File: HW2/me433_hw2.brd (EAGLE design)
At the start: 50 x 50 mm, 22 parts

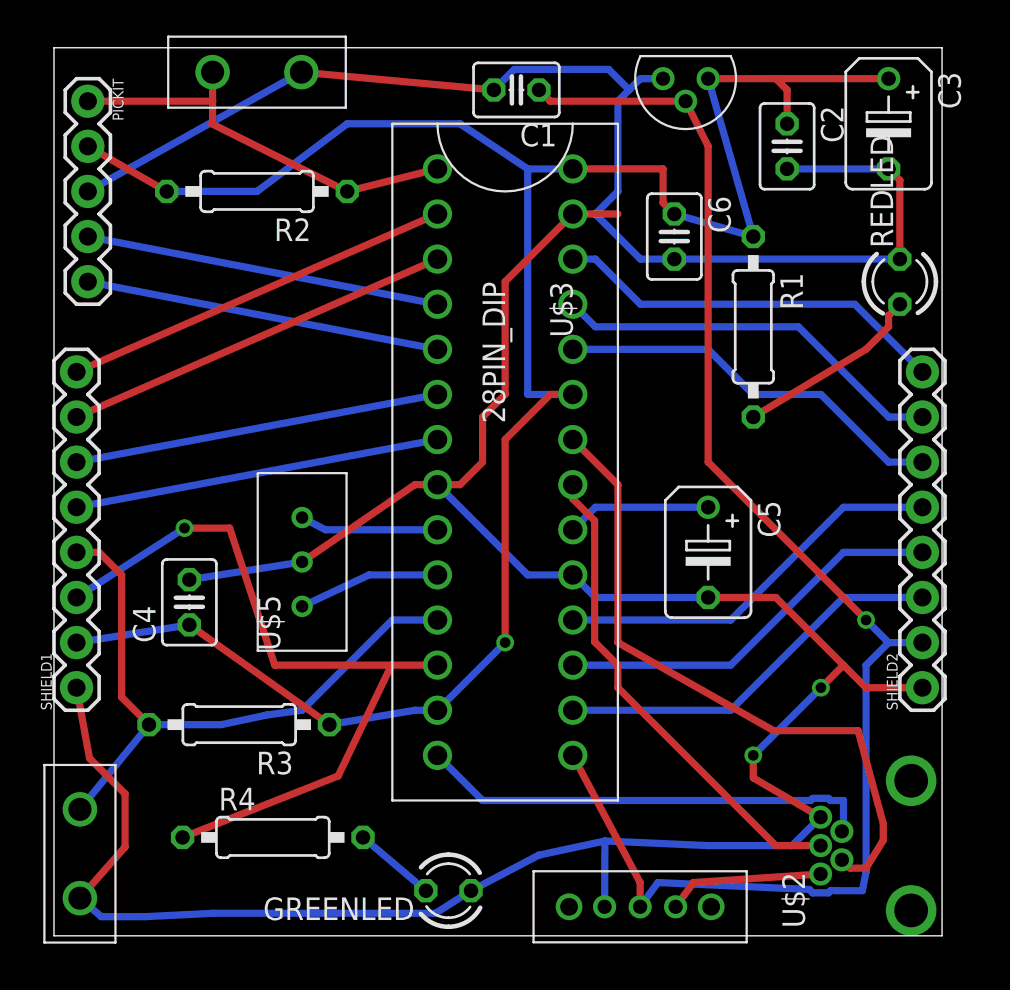
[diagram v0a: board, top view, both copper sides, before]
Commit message: added ground plane and fixed things
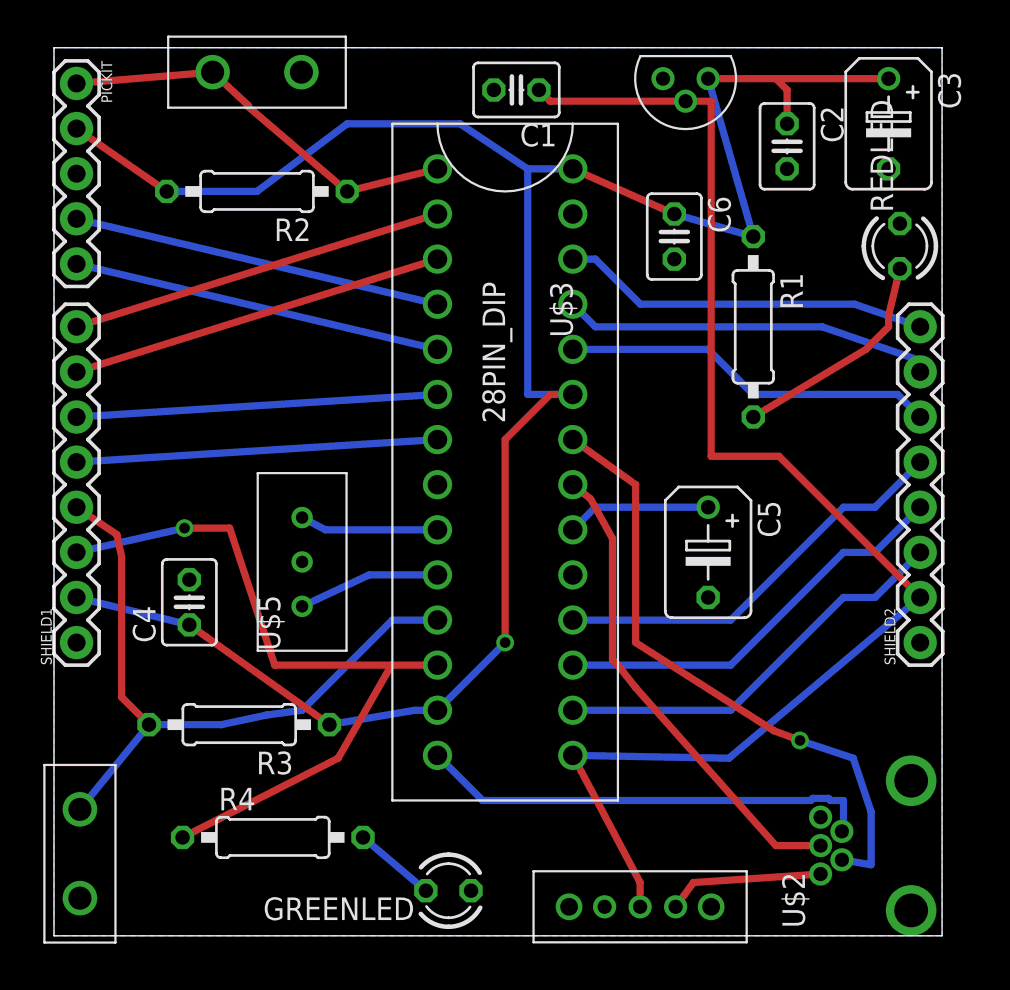
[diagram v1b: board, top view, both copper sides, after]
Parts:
- moved SHIELD2 2.54 mm to (48.8, 16.5)
- moved SHIELD1 2.54 mm to (1.27, 16.5)
- moved REDLED 2.00 mm to (47.6, 38.8)
- moved PICKIT 1.18 mm to (1.27, 48.0)
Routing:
- net GND: track 216.7 -> 0.00 mm, vias 2 -> 0
- net +5V: track 82.6 -> 77.3 mm, vias 1 -> 0
- net D-: track 37.1 -> 35.0 mm, vias 0 -> 1
- net B4: track 36.7 -> 38.7 mm
- net N$1: track 10.7 -> 12.5 mm
- net B15: track 22.3 -> 20.8 mm
- net A4: track 43.4 -> 41.9 mm
- net B14: track 22.2 -> 21.0 mm
- net B9: track 22.2 -> 23.2 mm
- net B8: track 22.2 -> 23.2 mm
- net B7: track 22.2 -> 23.2 mm
- net A1: track 22.2 -> 21.3 mm
- net A0: track 22.2 -> 21.3 mm
- net B13: track 22.2 -> 21.3 mm
- net PGD1: track 20.1 -> 20.9 mm
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- added copper zone on layer 16, net GND

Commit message: finished pcb and gerber files
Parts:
- moved GREENLED 12.4 mm to (9.79, 2.46), turned to 0 degrees
- moved U$4 7.22 mm to (25.8, 2.23)
- moved U$2 2.52 mm to (45.8, 5.38)
- moved R4 2.24 mm to (11.3, 7.54)
- moved USER 1.41 mm to (2.46, 5.62)
- moved RESET 1.00 mm to (11.4, 47.6)
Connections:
- net GND: no longer U$4.RIGHT
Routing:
- net USBID: track 25.8 -> 32.9 mm, vias 0 -> 1
- net SLIDESWITCH: track 8.87 -> 14.0 mm
- net D-: track 35.0 -> 31.3 mm, vias 1 -> 0
- net N$6: track 4.64 -> 7.37 mm
- net D+: track 27.1 -> 24.9 mm
- net B4: track 38.7 -> 37.3 mm
- net A4: track 41.9 -> 43.2 mm
- net +5V: track 77.3 -> 76.5 mm
- net MCLR: track 23.1 -> 22.5 mm
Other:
- board text added: "3V3"
- board text added: "5V"
- board text added: "A0"
- board text added: "A1"
- board text added: "A4"
- board text added: "B13"
- board text added: "B14"
- board text added: "B15"
- board text added: "B2"
- board text added: "B3"
- board text added: "B4"
- board text added: "B7"
- board text added: "B8"
- board text added: "B9"
- board text added: "GND"
- board text added: "GREEN"
- board text added: "Joseph"
- board text added: "MCLR"
- board text added: "ME433"
- board text added: "ON"
- board text added: "PGC1"
- board text added: "PGD1"
- board text added: "PIC32"
- board text added: "RED"
- board text added: "RESET"
- board text added: "Sombeck"
- board text added: "USER"
- board text added: "VIN"
- board text added: "VOUT"
